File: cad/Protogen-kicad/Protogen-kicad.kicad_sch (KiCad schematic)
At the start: 7 parts, among them M1 Fan, Q1 TIP122, U1 ESP32-S3, U2 LM2596S-5

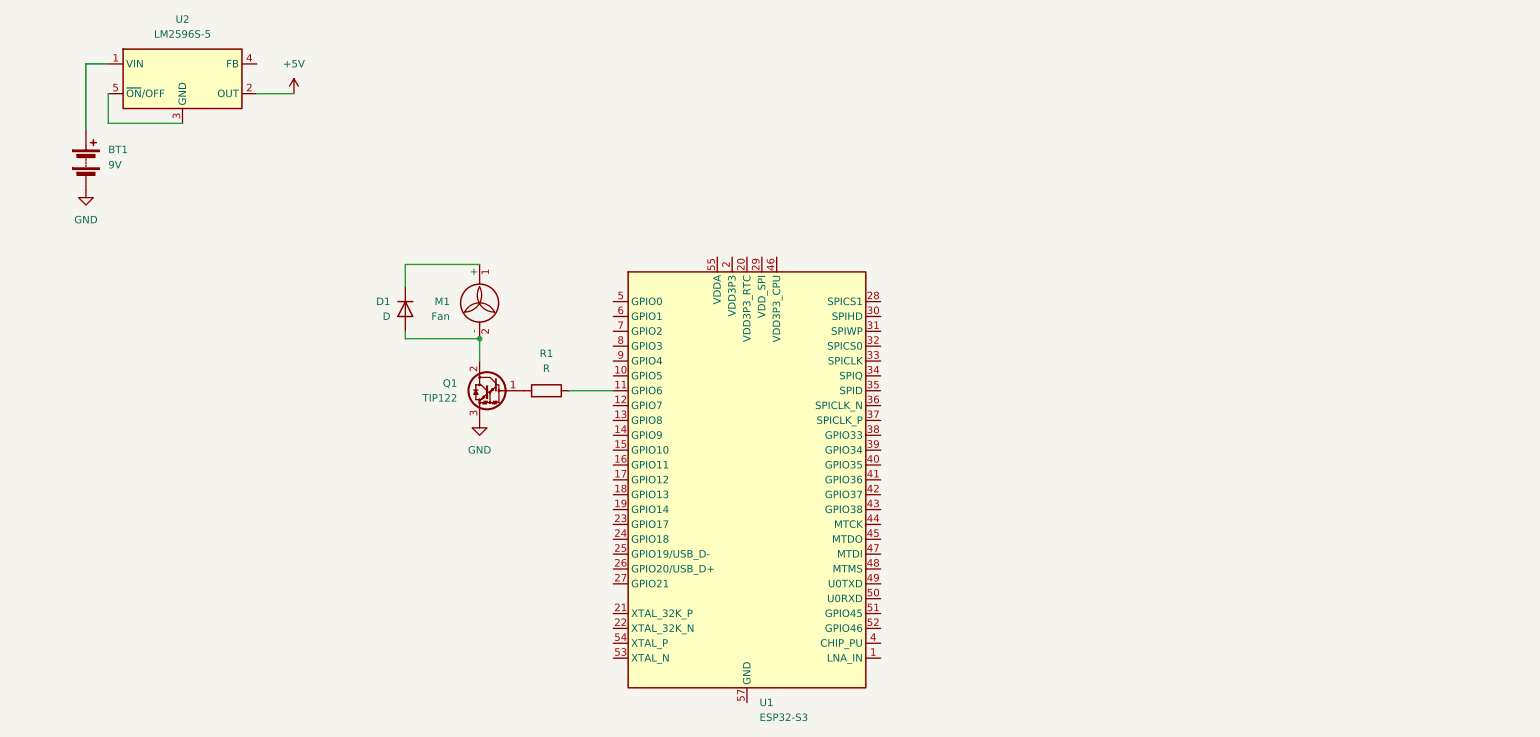
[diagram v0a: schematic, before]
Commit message: esquemático da proof of concept
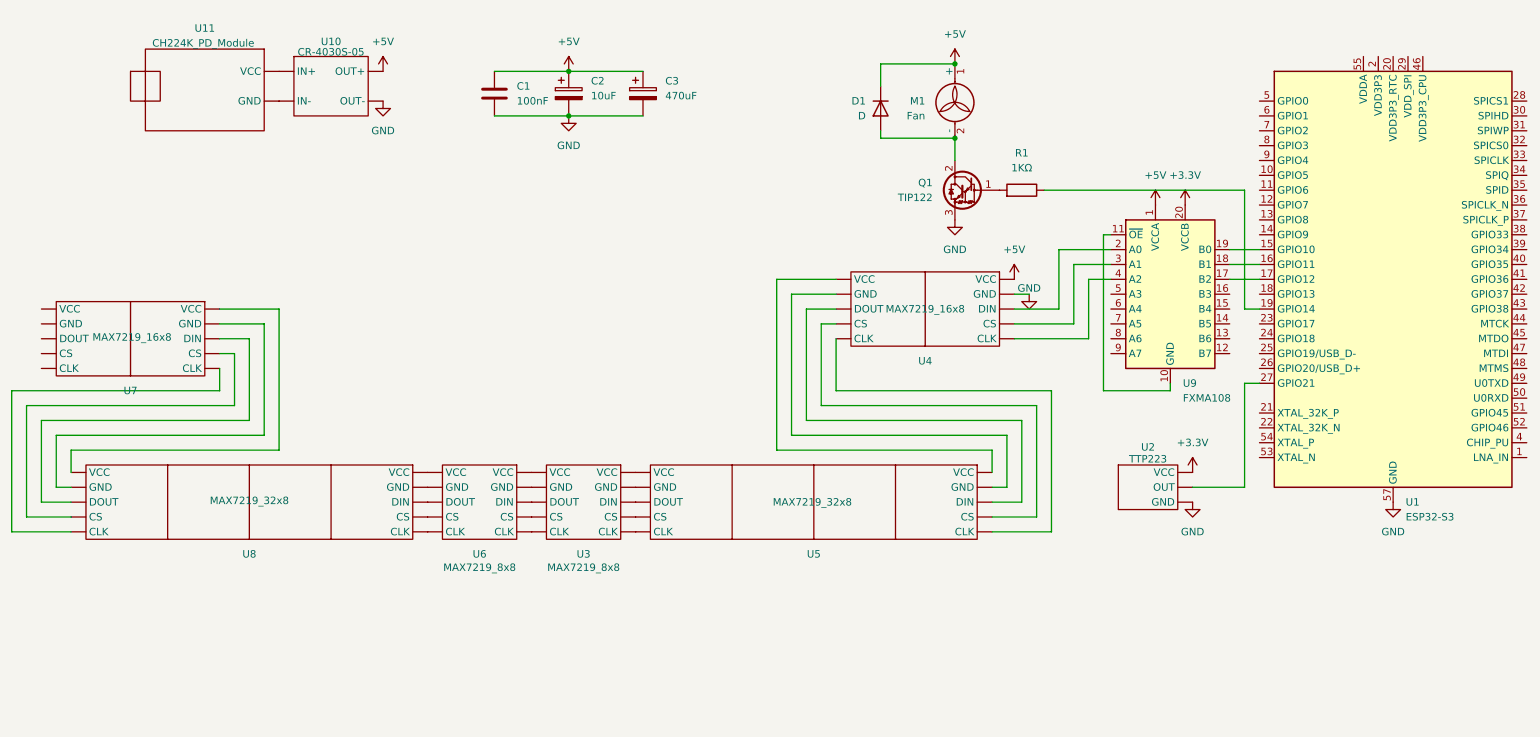
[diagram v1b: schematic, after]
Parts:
- removed BT1: 9V, symbol Device:Battery
- removed U2: LM2596S-5, Package_TO_SOT_SMD:TO-263-5_TabPin3, symbol Regulator_Switching:LM2596S-5
- added C1: 100nF, symbol Device:C
- added C2: 10uF, symbol Device:C_Polarized
- added C3: 470uF, symbol Device:C_Polarized
- added U10: CR-4030S-05, symbol New_Library:CR-4030S-05
- added U11: CH224K_PD_Module, symbol New_Library:ch224k_PD_Module
- added U2: TTP223, symbol New_Library:TTP223
- added U3, U6: MAX7219_8x8, symbol New_Library:MAX7219_8x8_LEDMatrix
- added U4, U7: MAX7219_16x8, symbol New_Library:MAX7219_16x8_LEDMatrix
- added U5, U8: MAX7219_32x8, symbol New_Library:MAX7219_32x8_LEDMatrix
- added U9: FXMA108, Package_DFN_QFN:WQFN-20-1EP_2.5x4.5mm_P0.5mm_EP1x2.9mm, symbol Logic_LevelTranslator:FXMA108
- R1: value R -> 1KΩ
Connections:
- net +5V: now also D1.1 (K), M1.1 (+), C1.1, C2.1, C3.1, U10. (OUT-), U4. (CLK), U9.1 (VCCA)
- net GND: now also U1.57 (GND), C1.2, C2.2, C3.2, U10. (OUT-), U2. (GND), U4. (CLK)
- net at R1.1: now also U1.19 (GPIO14); no longer U1.11 (GPIO6)
- net at U1.15 (GPIO10): now also U9.19 (B0)
- net at U1.16 (GPIO11): now also U9.18 (B1)
- net at U1.17 (GPIO12): now also U9.17 (B2)
- net at U1.27 (GPIO21): now also U2. (GND)
- new net: U10. (OUT-), U11. (GND) (x2)
- new net: U9.10 (GND), U9.11 (~{OE})
- new net: U4. (CLK), U9.2 (A0)
- new net: U4. (CLK), U9.3 (A1)
- new net: U4. (CLK), U9.4 (A2)
- new net: U7. (CLK), U8. (CLK) (x5)
- new net: U6. (CLK), U8. (CLK) (x5)
- new net: U4. (CLK), U5. (CLK) (x5)
- new net: U3. (CLK), U5. (CLK) (x5)
- new net: U3. (CLK), U6. (CLK) (x5)
- new net +3.3V: U2. (GND), U9.20 (VCCB)
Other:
- moved on the sheet: D1, M1, Q1, R1, U1
